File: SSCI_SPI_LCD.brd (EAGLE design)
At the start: 110 x 100 mm, 30 parts, among them IC3 74LVC541_RGY, X1 TSW-108-02-S-S, X2 TSW-108-02-S-S

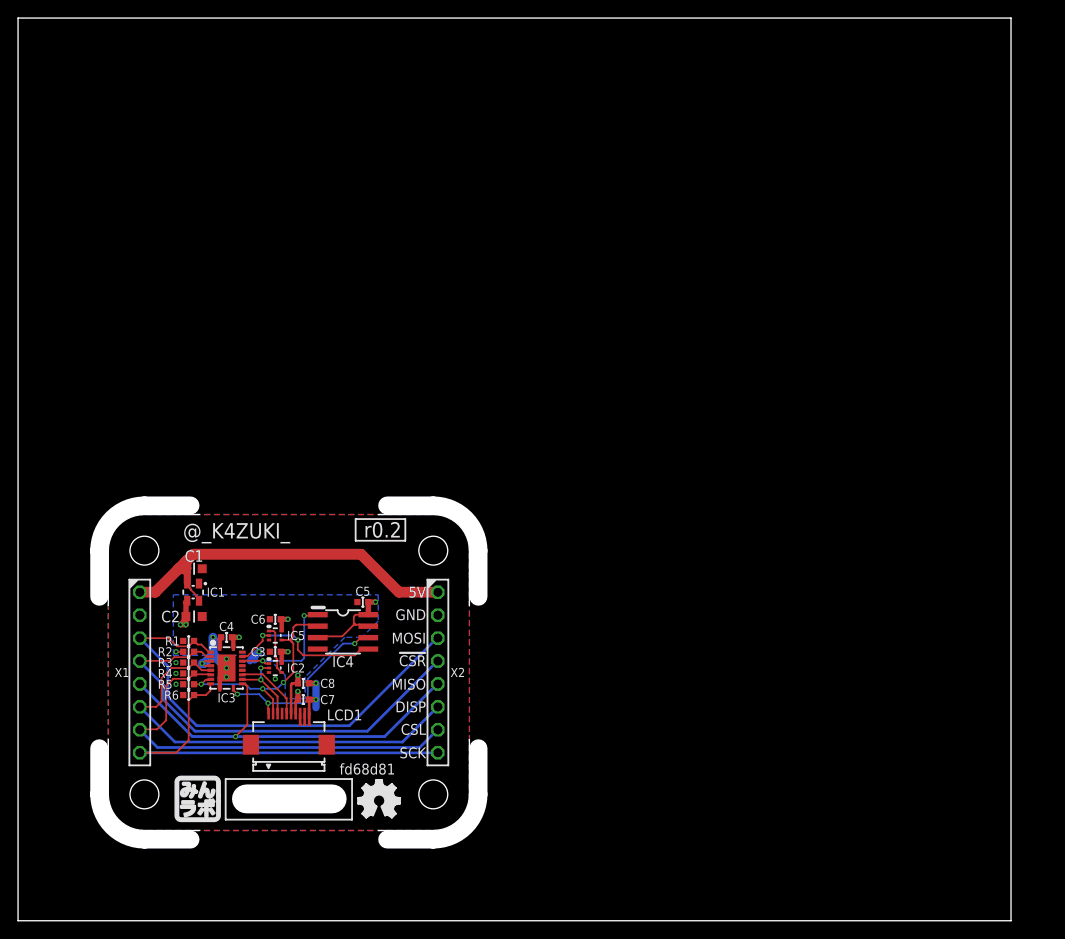
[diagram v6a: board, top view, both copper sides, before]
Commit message: [ BRD ] add fiducial
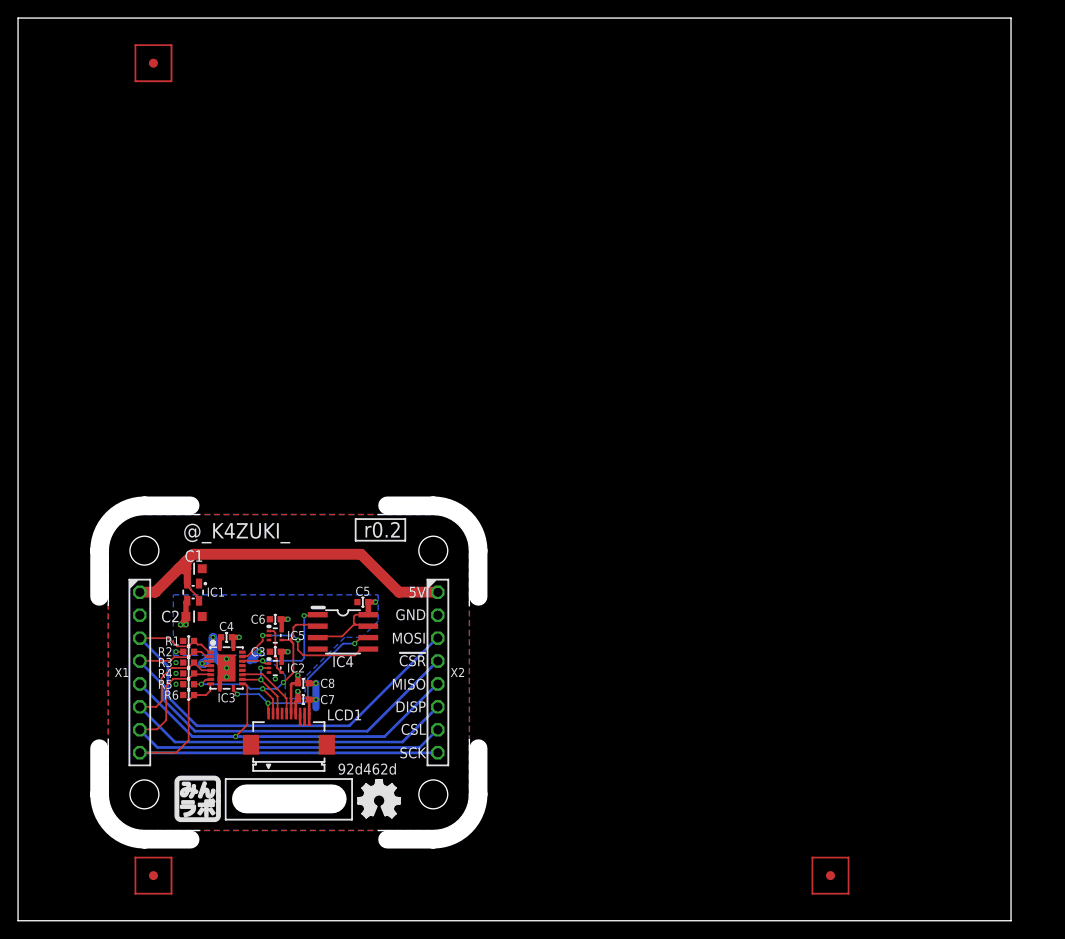
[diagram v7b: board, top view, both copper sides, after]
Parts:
- added TP1, TP2, TP3: (no value), mylib:FIDUCIAL
- GIT1: value fd68d81 -> 92d462d
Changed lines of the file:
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@@
 <layer number="100" name="Muster" color="7" fill="1" visible="no" active="no"/>
 <layer number="101" name="Attributes" color="7" fill="1" visible="no" active="yes"/>
-<layer number="102" name="Vscore" color="7" fill="1" visible="no" active="yes"/>
+<layer number="102" name="Vscore" color="7" fill="1" visible="yes" active="yes"/>
 <layer number="103" name="tMap" color="7" fill="1" visible="no" active="yes"/>
 <layer number="104" name="Name" color="7" fill="1" visible="no" active="yes"/>
@@
 <attribute name="NOT_COMPONENT" value="YES" x="14" y="14" size="1.778" layer="27" rot="R270" display="off"/>
 </element>
-<element name="GIT1" library="git-revision" package="GIT-REVISION_1.2" value="fd68d81" x="38.7" y="16.8">
+<element name="GIT1" library="git-revision" package="GIT-REVISION_1.2" value="92d462d" x="38.7" y="16.8">
 <attribute name="NOT_COMPONENT" value="YES" x="38.7" y="16.8" size="1.778" layer="27" display="off"/>
 </element>
@@
 <attribute name="NOT_COMPONENT" value="YES" x="17.4" y="11" size="1.2" layer="27" ratio="20" display="off"/>
 </element>
+<element name="TP1" library="mylib" package="FIDUCIAL" value="" x="15" y="5">
+<attribute name="NOT_COMPONENT" value="YES" x="15" y="5" size="1.778" layer="27" display="off"/>
+</element>
+<element name="TP2" library="mylib" package="FIDUCIAL" value="" x="90" y="5">
+<attribute name="NOT_COMPONENT" value="YES" x="90" y="5" size="1.778" layer="27" display="off"/>
+</element>
+<element name="TP3" library="mylib" package="FIDUCIAL" value="" x="15" y="95">
+<attribute name="NOT_COMPONENT" value="YES" x="15" y="95" size="1.778" layer="27" display="off"/>
+</element>
 </elements>

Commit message: [ BRD ] replace pinheader; revision 0.3; add corner 4.0mm holes
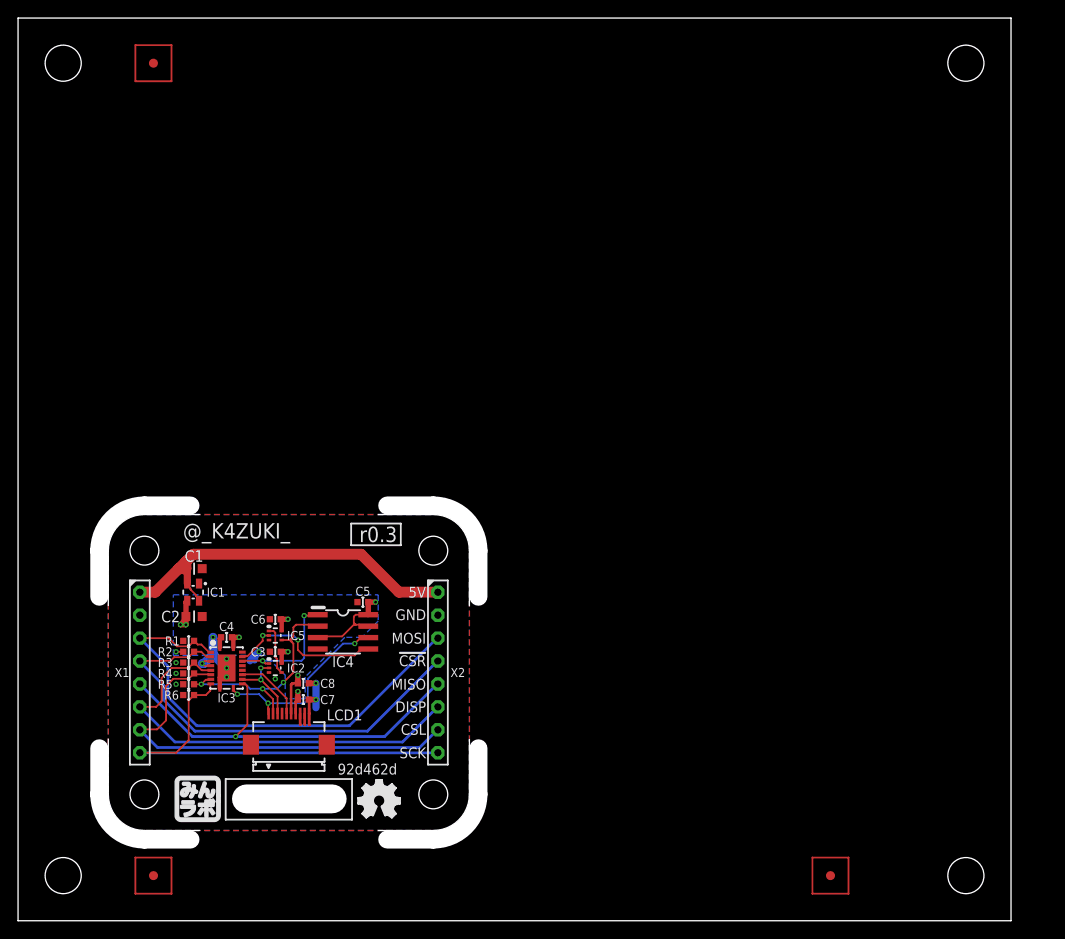
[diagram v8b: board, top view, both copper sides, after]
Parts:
- ICON1: value r0.2 -> r0.3
- X1, X2: value TSW-108-02-S-S -> PHA-1X08SG; device con-samtec.local:TSW-108-02-S-S -> mylib:PHA-1X08SG
- moved ICON1 0.71 mm to (40.0, 42.8)
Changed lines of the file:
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@@
 <dimension x1="13.49" y1="27.5" x2="46.51" y2="27.5" x3="30" y3="2.9" textsize="1.2" textratio="20" layer="47" dtype="horizontal" unit="inch" visible="yes"/>
 <wire x1="31.9" y1="24.1" x2="32.5" y2="24.1" width="0" layer="41"/>
+<hole x="5" y="5" drill="4"/>
+<hole x="105" y="5" drill="4"/>
+<hole x="105" y="95" drill="4"/>
+<hole x="5" y="95" drill="4"/>
 </plain>
 <attributes>
@@
 <attribute name="NOT_COMPONENT" value="YES" x="38.7" y="16.8" size="1.778" layer="27" display="off"/>
 </element>
-<element name="ICON1" library="mylib" package="ICON_REVISION1.7" value="r0.2" x="40.5" y="43.3">
-<attribute name="NOT_COMPONENT" value="YES" x="40.5" y="43.3" size="1.778" layer="27" display="off"/>
-</element>
-<element name="X1" library="con-samtec.local" package="TSW-108-02-S-S" value="TSW-108-02-S-S" x="13.49" y="27.5" smashed="yes" rot="R90">
+<element name="ICON1" library="mylib" package="ICON_REVISION1.7" value="r0.3" x="40" y="42.8">
+<attribute name="NOT_COMPONENT" value="YES" x="40" y="42.8" size="1.778" layer="27" display="off"/>
+</element>
+<element name="X1" library="mylib" package="PHA-1X08SG" value="PHA-1X08SG" x="13.49" y="27.5" smashed="yes" rot="R90">
 <attribute name="NAME" x="12.33" y="27.5" size="1" layer="25" ratio="20" align="center-right"/>
 <attribute name="VALUE" x="14.69" y="39.5" size="1" layer="27" ratio="20" rot="R180"/>
-</element>
-<element name="X2" library="con-samtec.local" package="TSW-108-02-S-S" value="TSW-108-02-S-S" x="46.51" y="27.5" smashed="yes" rot="R90">
+<attribute name="AKIZUKI" value="C-04394" x="13.49" y="27.5" size="1.778" layer="27" rot="R90" display="off"/>
+</element>
+<element name="X2" library="mylib" package="PHA-1X08SG" value="PHA-1X08SG" x="46.51" y="27.5" smashed="yes" rot="R90">
 <attribute name="NAME" x="47.9" y="27.5" size="1" layer="25" ratio="20" rot="R180" align="center-right"/>
 <attribute name="VALUE" x="47.71" y="39.5" size="1" layer="27" ratio="20" rot="R180"/>
+<attribute name="AKIZUKI" value="C-04394" x="46.51" y="27.5" size="1.778" layer="27" rot="R90" display="off"/>
 </element>
 <element name="IC4" library="mylib" package="IC_08_1.27_150MIL" value="" x="36" y="32" smashed="yes" rot="R270">
